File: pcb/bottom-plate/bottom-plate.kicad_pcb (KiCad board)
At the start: 2 copper layers, 285.8 x 114.3 mm, 16 parts

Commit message: Update bottom plate silkscreens
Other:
- board text added: "RESET"
- board text added: "USB BOOT"
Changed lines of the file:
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@@
     (tags "mounting hole 2.2mm no annular m2")
     (attr exclude_from_pos_files exclude_from_bom)
-    (fp_text reference "REF**" (at 0 -3.2) (layer "F.SilkS")
+    (fp_text reference "REF**" (at 0 -3.2) (layer "F.SilkS") hide
       (effects (font (size 1 1) (thickness 0.15)))
     )
@@
     (tags "mounting hole 2.2mm no annular m2")
     (attr exclude_from_pos_files exclude_from_bom)
-    (fp_text reference "REF**" (at 0 -3.2) (layer "F.SilkS")
+    (fp_text reference "REF**" (at 0 -3.2) (layer "F.SilkS") hide
       (effects (font (size 1 1) (thickness 0.15)))
     )
@@
     (tags "mounting hole 2.2mm no annular m2")
     (attr exclude_from_pos_files exclude_from_bom)
-    (fp_text reference "REF**" (at 0 -3.2) (layer "F.SilkS")
+    (fp_text reference "REF**" (at 0 -3.2) (layer "F.SilkS") hide
       (effects (font (size 1 1) (thickness 0.15)))
     )
@@
     (tags "mounting hole 3.2mm no annular m3")
     (attr exclude_from_pos_files exclude_from_bom)
-    (fp_text reference "REF**" (at 0 -4.2) (layer "F.SilkS")
+    (fp_text reference "REF**" (at 0 -4.2) (layer "F.SilkS") hide
       (effects (font (size 1 1) (thickness 0.15)))
     )
@@
     (tags "mounting hole 2.2mm no annular m2")
     (attr exclude_from_pos_files exclude_from_bom)
-    (fp_text reference "REF**" (at 0 -3.2) (layer "F.SilkS")
+    (fp_text reference "REF**" (at 0 -3.2) (layer "F.SilkS") hide
       (effects (font (size 1 1) (thickness 0.15)))
     )
@@
     (tags "mounting hole 3.2mm no annular m3")
     (attr exclude_from_pos_files exclude_from_bom)
-    (fp_text reference "REF**" (at 0 -4.2) (layer "F.SilkS")
+    (fp_text reference "REF**" (at 0 -4.2) (layer "F.SilkS") hide
       (effects (font (size 1 1) (thickness 0.15)))
     )
@@
     (tags "mounting hole 2.2mm no annular m2")
     (attr exclude_from_pos_files exclude_from_bom)
-    (fp_text reference "REF**" (at 0 -3.2) (layer "F.SilkS")
+    (fp_text reference "REF**" (at 0 -3.2) (layer "F.SilkS") hide
       (effects (font (size 1 1) (thickness 0.15)))
     )
@@
     (tags "mounting hole 2.2mm no annular m2")
     (attr exclude_from_pos_files exclude_from_bom)
-    (fp_text reference "REF**" (at 0 -3.2) (layer "F.SilkS")
+    (fp_text reference "REF**" (at 0 -3.2) (layer "F.SilkS") hide
       (effects (font (size 1 1) (thickness 0.15)))
     )
@@
     (tags "mounting hole 2.2mm no annular m2")
     (attr exclude_from_pos_files exclude_from_bom)
-    (fp_text reference "REF**" (at 0 -3.2) (layer "F.SilkS")
+    (fp_text reference "REF**" (at 0 -3.2) (layer "F.SilkS") hide
       (effects (font (size 1 1) (thickness 0.15)))
     )
@@
     (tags "mounting hole 2.2mm no annular m2")
     (attr exclude_from_pos_files exclude_from_bom)
-    (fp_text reference "REF**" (at 0 -3.2) (layer "F.SilkS")
+    (fp_text reference "REF**" (at 0 -3.2) (layer "F.SilkS") hide
       (effects (font (size 1 1) (thickness 0.15)))
     )
@@
     (tags "mounting hole 2.2mm no annular m2")
     (attr exclude_from_pos_files exclude_from_bom)
-    (fp_text reference "REF**" (at 0 -3.2) (layer "F.SilkS")
+    (fp_text reference "REF**" (at 0 -3.2) (layer "F.SilkS") hide
       (effects (font (size 1 1) (thickness 0.15)))
     )
@@
     (tags "mounting hole 2.2mm no annular m2")
     (attr exclude_from_pos_files exclude_from_bom)
-    (fp_text reference "REF**" (at 0 -3.2) (layer "F.SilkS")
+    (fp_text reference "REF**" (at 0 -3.2) (layer "F.SilkS") hide
       (effects (font (size 1 1) (thickness 0.15)))
     )
@@
     (tags "mounting hole 3.2mm no annular m3")
     (attr exclude_from_pos_files exclude_from_bom)
-    (fp_text reference "REF**" (at 0 -4.2) (layer "F.SilkS")
+    (fp_text reference "REF**" (at 0 -4.2) (layer "F.SilkS") hide
       (effects (font (size 1 1) (thickness 0.15)))
     )
@@
     (tags "mounting hole 2.2mm no annular m2")
     (attr exclude_from_pos_files exclude_from_bom)
-    (fp_text reference "REF**" (at 0 -3.2) (layer "F.SilkS")
+    (fp_text reference "REF**" (at 0 -3.2) (layer "F.SilkS") hide
       (effects (font (size 1 1) (thickness 0.15)))
     )
@@
     (tags "mounting hole 2.2mm no annular m2")
     (attr exclude_from_pos_files exclude_from_bom)
-    (fp_text reference "REF**" (at 0 -3.2) (layer "F.SilkS")
+    (fp_text reference "REF**" (at 0 -3.2) (layer "F.SilkS") hide
       (effects (font (size 1 1) (thickness 0.15)))
     )
@@
     (tags "mounting hole 3.2mm no annular m3")
     (attr exclude_from_pos_files exclude_from_bom)
-    (fp_text reference "REF**" (at 0 -4.2) (layer "F.SilkS")
+    (fp_text reference "REF**" (at 0 -4.2) (layer "F.SilkS") hide
       (effects (font (size 1 1) (thickness 0.15)))
     )
@@
   (gr_line (start 304.8 21.4313) (end 304.8 130.9688) (layer "Edge.Cuts") (width 0.1))
   (gr_arc (start 304.8 130.9688) (mid 304.102516 132.652551) (end 302.41875 133.35005) (layer "Edge.Cuts") (width 0.1))
+  (gr_text "USB BOOT" (at 62.1 73) (layer "B.SilkS")
+    (effects (font (size 1 1) (thickness 0.15)) (justify mirror))
+  )
+  (gr_text "RESET" (at 33.1 105.5) (layer "B.SilkS")
+    (effects (font (size 1 1) (thickness 0.15)) (justify mirror))
+  )
   (gr_text "key-ripper-bottom-plate\nv0.3" (at 185.8 115.4188) (layer "F.SilkS")
     (effects (font (size 1 1) (thickness 0.15)))

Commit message: Use the copper pour on the bottom plate on both sides
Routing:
- added copper zone on B.Cu, net (none)
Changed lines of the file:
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@@
     (effects (font (size 1 1) (thickness 0.15)))
   )
-  (zone (net 0) (net_name "") (layer "F.Cu") (hatch edge 0.508)
+  (zone (net 0) (net_name "") (layers F&B.Cu) (hatch edge 0.508)
     (connect_pads (clearance 0.508))
     (min_thickness 0.254) (filled_areas_thickness no)

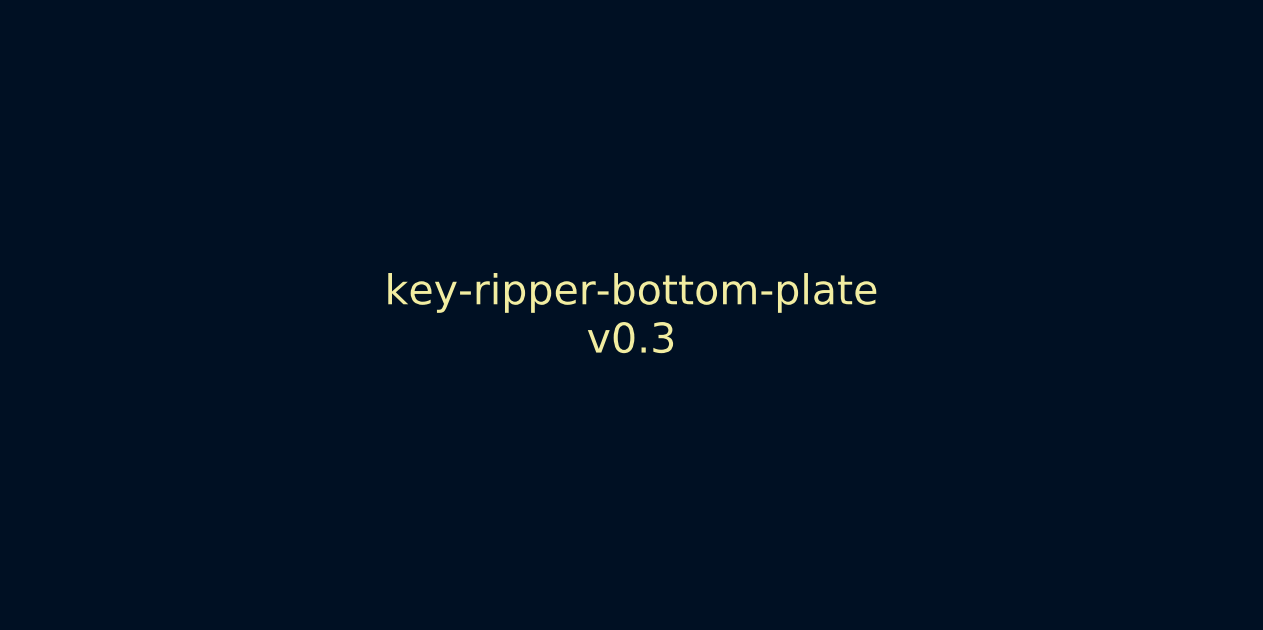
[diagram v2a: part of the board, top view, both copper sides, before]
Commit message: Update silkscreens on the plates
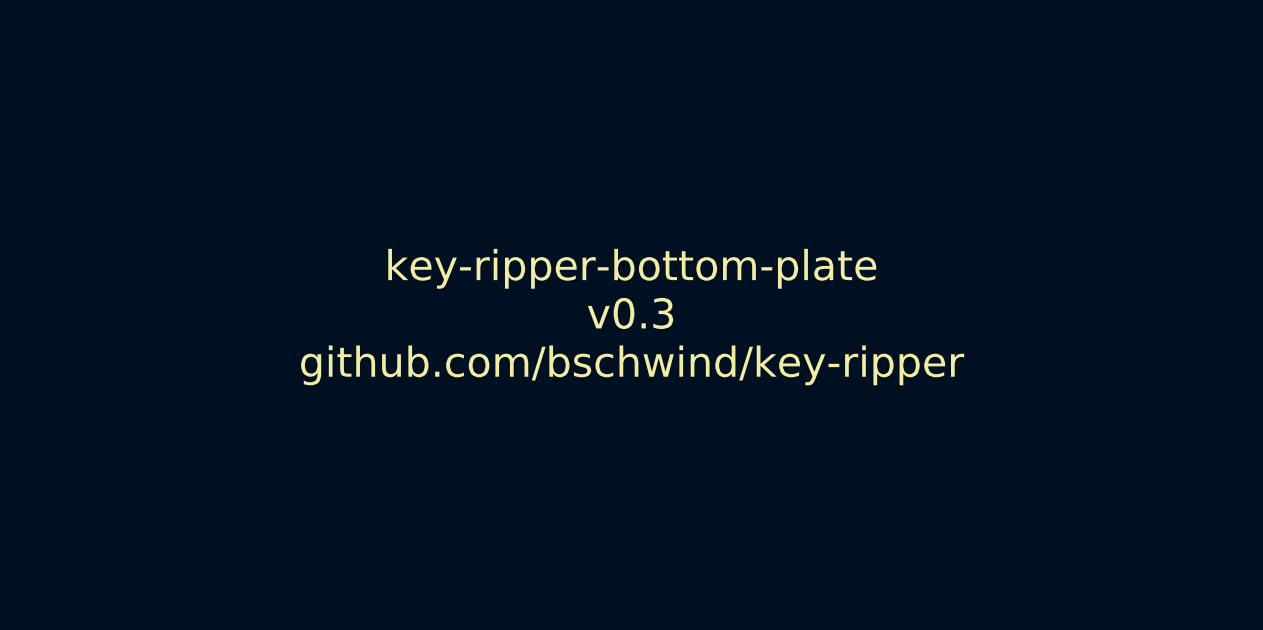
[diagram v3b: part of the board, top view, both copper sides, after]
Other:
- board text added: "key-ripper-bottom-plate v0.3 github.com/bschwind/key-ripper"
- board text removed: "key-ripper-bottom-plate v0.3"
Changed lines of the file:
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@@
     (effects (font (size 1 1) (thickness 0.15)) (justify mirror))
   )
-  (gr_text "key-ripper-bottom-plate\nv0.3" (at 185.8 115.4188) (layer "F.SilkS")
+  (gr_text "key-ripper-bottom-plate\nv0.3\ngithub.com/bschwind/key-ripper" (at 185.8 115.4188) (layer "F.SilkS")
     (effects (font (size 1 1) (thickness 0.15)))
   )
